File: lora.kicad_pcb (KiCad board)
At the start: 2 copper layers, 1 part, among them U1 SX1301

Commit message: partialy wired - sequential pins
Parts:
- added C2: 100nF, Capacitor_SMD:C_0603_1608Metric_Pad1.05x0.95mm_HandSolder, F.Cu at (154.5, 92.2)
- added C3: 100nF, Capacitor_SMD:C_0603_1608Metric_Pad1.05x0.95mm_HandSolder, F.Cu at (154.1, 88.9)
- added C4: 100nF, Capacitor_SMD:C_0603_1608Metric_Pad1.05x0.95mm_HandSolder, F.Cu at (157.9, 111.8)
- added C5: 100n, Capacitor_SMD:C_0603_1608Metric_Pad1.05x0.95mm_HandSolder, F.Cu at (158.4, 109.2)
- added C6: 100nF, Capacitor_SMD:C_0603_1608Metric_Pad1.05x0.95mm_HandSolder, F.Cu at (165.5, 100.7)
- added C7: 100n, Capacitor_SMD:C_0603_1608Metric_Pad1.05x0.95mm_HandSolder, F.Cu at (167.6, 100.7)
- added J1: Conn_01x10_Male, Connector_PinHeader_2.54mm:PinHeader_1x10_P2.54mm_Vertical, F.Cu at (139.0, 90.7)
- added R1: 10k, Resistor_SMD:R_0603_1608Metric_Pad1.05x0.95mm_HandSolder, F.Cu at (147.3, 100.7)
- added R10: 100, Resistor_SMD:R_0603_1608Metric_Pad1.05x0.95mm_HandSolder, F.Cu at (174.4, 95.2)
- added R2: 10k, Resistor_SMD:R_0603_1608Metric_Pad1.05x0.95mm_HandSolder, F.Cu at (146.8, 90.2)
- added R3: 100, Resistor_SMD:R_0603_1608Metric_Pad1.05x0.95mm_HandSolder, F.Cu at (174.4, 102.9)
- added R4: 100, Resistor_SMD:R_0603_1608Metric_Pad1.05x0.95mm_HandSolder, F.Cu at (178.2, 101.6)
- added R5: R, Resistor_SMD:R_0603_1608Metric_Pad1.05x0.95mm_HandSolder, F.Cu at (174.4, 100.3)
- added R6: 100, Resistor_SMD:R_0603_1608Metric_Pad1.05x0.95mm_HandSolder, F.Cu at (183.3, 100.3)
- added R7: 100, Resistor_SMD:R_0603_1608Metric_Pad1.05x0.95mm_HandSolder, F.Cu at (178.2, 99.1)
- added R8: 100, Resistor_SMD:R_0603_1608Metric_Pad1.05x0.95mm_HandSolder, F.Cu at (174.4, 97.8)
- added R9: 100, Resistor_SMD:R_0603_1608Metric_Pad1.05x0.95mm_HandSolder, F.Cu at (178.2, 96.5)
- moved U1 92.7 mm to (155.0, 100.4)
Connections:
- U1 pad 1: Net-(U1-Pad1) -> /RESET
- U1 pad 12: Net-(U1-Pad12) -> +1V8
- U1 pad 16: Net-(U1-Pad16) -> Earth
- U1 pad 2: Net-(U1-Pad2) -> /HOST_SCK
- U1 pad 23: Net-(U1-Pad23) -> +1V8
- U1 pad 29: Net-(U1-Pad29) -> +3V3
- U1 pad 32: Net-(U1-Pad32) -> Earth
- U1 pad 33: Net-(U1-Pad33) -> Earth
- U1 pad 34: Net-(U1-Pad34) -> Earth
- U1 pad 42: Net-(U1-Pad42) -> +1V8
- U1 pad 48: Net-(U1-Pad48) -> Earth
- U1 pad 49: Net-(U1-Pad49) -> Earth
- U1 pad 52: Net-(U1-Pad52) -> +3V3
- U1 pad 6: Net-(U1-Pad6) -> Earth
- U1 pad 60: Net-(U1-Pad60) -> +1V8
- U1 pad 8: Net-(U1-Pad8) -> +1V8
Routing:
- net +1V8: track 0.00 -> 3.21 mm
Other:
- net class 1V8 added: clearance 0.2, trace_width 0.25, via_dia 0.8, via_drill 0.4
- net class 3V3 added: clearance 0.2, trace_width 0.25, via_dia 0.8, via_drill 0.4

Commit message: v1.0
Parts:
- added C1: 1uF, Capacitor_SMD:C_0603_1608Metric, F.Cu at (134.6, 43.4)
- added C10: 2n2, Capacitor_SMD:C_0402_1005Metric, F.Cu at (114.7, 33.4)
- added C11: 22u, Capacitor_SMD:C_0603_1608Metric, F.Cu at (116.2, 45.1)
- added C12: 100nF, Capacitor_SMD:C_0402_1005Metric, F.Cu at (124.9, 56.7)
- added C8: 1u, Capacitor_SMD:C_0603_1608Metric, F.Cu at (114.2, 35.2)
- added C9: 10u, Capacitor_SMD:C_0603_1608Metric, F.Cu at (132.1, 40.4)
- added D1: LED, LED_SMD:LED_0402_1005Metric, F.Cu at (124.3, 34.7)
- added D2: LED, LED_SMD:LED_0402_1005Metric, F.Cu at (125.0, 36.9)
- added D3: LED, LED_SMD:LED_0402_1005Metric, F.Cu at (125.7, 34.7)
- added D4: LED, LED_SMD:LED_0402_1005Metric, F.Cu at (126.4, 36.9)
- added D5: LED, LED_SMD:LED_0402_1005Metric, F.Cu at (127.1, 34.7)
- added J2: Conn_Coaxial, Connector_Coaxial:U.FL_Molex_MCRF_73412-0110_Vertical, F.Cu at (116.2, 58.5)
- added J3: Conn_01x08_Male, Connector_PinHeader_2.54mm:PinHeader_1x08_P2.54mm_Vertical, B.Cu at (114.3, 63.5)
- added J4: Conn_01x10_Male, Connector_PinHeader_2.54mm:PinHeader_1x10_P2.54mm_Vertical, B.Cu at (139.7, 61.0)
- added J5: Conn_01x06_Male, Connector_PinHeader_2.54mm:PinHeader_1x06_P2.54mm_Vertical, B.Cu at (127.0, 30.5)
- added L1: 2.2uH, Inductor_SMD:L_6.3x6.3_H3, F.Cu at (117.5, 40.5)
- added R11: 100k, Resistor_SMD:R_0402_1005Metric, F.Cu at (121.0, 34.5)
- added R12: 100, Resistor_SMD:R_0402_1005Metric, F.Cu at (133.3, 56.7)
- added R13: 470, Resistor_SMD:R_0402_1005Metric, F.Cu at (127.1, 39.3)
- added R14: 470, Resistor_SMD:R_0402_1005Metric, F.Cu at (126.4, 41.8)
- added R15: 470, Resistor_SMD:R_0402_1005Metric, F.Cu at (125.7, 39.3)
- added R16: 470, Resistor_SMD:R_0402_1005Metric, F.Cu at (125.0, 41.9)
- added R17: 470, Resistor_SMD:R_0402_1005Metric, F.Cu at (124.3, 39.3)
- added R18: 0, Resistor_SMD:R_0402_1005Metric, F.Cu at (137.6, 53.0)
- added TP1: TestPoint, TestPoint:TestPoint_THTPad_1.5x1.5mm_Drill0.7mm, F.Cu at (131.7, 43.3)
- added TP3: TestPoint, TestPoint:TestPoint_THTPad_1.5x1.5mm_Drill0.7mm, F.Cu at (128.9, 39.8)
- added U2: TPS62141, Package_DFN_QFN:QFN-16-1EP_3x3mm_P0.5mm_EP1.8x1.8mm, F.Cu at (118.0, 34.5)
- added X1: DFA-S15, Oscillator:Oscillator_SMD_Fordahl_DFAS15-4Pin_5.0x3.2mm, F.Cu at (134.6, 52.9)
- added X2: ASE-xxxMHz, Oscillator:Oscillator_SMD_Abracon_ASE-4Pin_3.2x2.5mm, F.Cu at (130.9, 36.8)
- C2, C3, C4, C5, C6, C7: footprint Capacitor_SMD:C_0603_1608Metric_Pad1.05x0.95mm_HandSolder -> Capacitor_SMD:C_0402_1005Metric
- J1: moved to B.Cu
- R1, R10, R2, R3, R4, R6, R7, R8, R9: footprint Resistor_SMD:R_0603_1608Metric_Pad1.05x0.95mm_HandSolder -> Resistor_SMD:R_0402_1005Metric
- R5: value R -> 100; footprint Resistor_SMD:R_0603_1608Metric_Pad1.05x0.95mm_HandSolder -> Resistor_SMD:R_0402_1005Metric
- moved C4 77.4 mm to (123.6, 42.4), turned to 90 degrees
- moved C5 72.1 mm to (128.8, 43.5), turned to 0 degrees
- moved R6 70.8 mm to (134.4, 49.1), turned to 180 degrees
- moved R7 67.2 mm to (134.4, 48.1), turned to 180 degrees
- moved R9 66.8 mm to (134.4, 46.1), turned to 180 degrees
- moved R8 64.6 mm to (134.4, 47.1)
- moved R10 64.1 mm to (134.4, 45.1), turned to 180 degrees
- moved R2 62.7 mm to (113.4, 37.1), turned to 270 degrees
- moved R4 61.5 mm to (133.2, 59.6)
- moved C6 61.4 mm to (132.4, 49.0), turned to 0 degrees
- moved J1 59.3 mm to (111.6, 38.1), turned to 180 degrees
- moved R5 58.9 mm to (133.3, 58.1)
- moved U1 58.8 mm to (125.3, 49.6)
- moved C7 58.7 mm to (127.9, 57.4), turned to 270 degrees
- moved R3 58.7 mm to (133.2, 61.0)
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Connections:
- net /HOST_SCK renamed /SCK
- C2 pad 1: Earth -> +1V8
- C2 pad 2: +1V8 -> Earth
- C4 pad 1: +3V3 -> +1V8
- C5 pad 1: Earth -> +3V3
- C5 pad 2: +3V3 -> Earth
- C6 pad 1: Earth -> +1V8
- C6 pad 2: +1V8 -> Earth
- C7 pad 1: Earth -> +3V3
- C7 pad 2: +1V8 -> Earth
- J1 pad 10: Net-(J1-Pad10) -> /PA_G0
- J1 pad 3: Net-(J1-Pad3) -> /MISO
- J1 pad 4: Net-(J1-Pad4) -> /MOSI
- J1 pad 5: Net-(J1-Pad5) -> /CS
- J1 pad 6: Net-(J1-Pad6) -> /RA_EN
- J1 pad 7: Net-(J1-Pad7) -> /LA_CTR
- J1 pad 8: Net-(J1-Pad8) -> /PA_CTR
- J1 pad 9: Net-(J1-Pad9) -> /PA_G1
- R1 pad 1: Net-(J2-Pad1) -> Earth
- R1 pad 2: Earth -> Net-(J2-Pad1)
- U1 pad 13: Net-(U1-Pad13) -> /RA_EN
- U1 pad 14: Net-(U1-Pad14) -> /LA_CTR
- U1 pad 15: Net-(U1-Pad15) -> /PA_CTR
- U1 pad 17: Net-(U1-Pad17) -> /PA_G1
- U1 pad 18: Net-(U1-Pad18) -> /PA_G0
- U1 pad 3: Net-(U1-Pad3) -> /MISO
- U1 pad 34: Earth -> Net-(R3-Pad1)
- U1 pad 35: Net-(R3-Pad1) -> Net-(R4-Pad2)
- U1 pad 36: Net-(R4-Pad2) -> Net-(R5-Pad2)
- U1 pad 39: Net-(R5-Pad2) -> Net-(R12-Pad2)
- U1 pad 4: Net-(U1-Pad4) -> /MOSI
- U1 pad 5: Net-(U1-Pad5) -> /CS
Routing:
- net Earth: track 48.4 -> 213.0 mm, vias 0 -> 13
- net +1V8: track 3.21 -> 119.3 mm, vias 0 -> 8
- net +3V3: track 0.00 -> 76.6 mm, vias 0 -> 4
- net Net-(J5-Pad1): track 0.00 -> 18.1 mm
- net /RESET: track 0.00 -> 17.1 mm
- net Net-(J5-Pad4): track 0.00 -> 16.2 mm
- net Net-(J5-Pad2): track 0.00 -> 15.6 mm
- net Net-(J5-Pad3): track 0.00 -> 15.4 mm
- net /PA_G0: track 0.00 -> 14.8 mm
- net Net-(J3-Pad1): track 0.00 -> 14.4 mm
- net /SCK: track 0.00 -> 13.6 mm
- net Net-(J2-Pad1): track 0.00 -> 13.3 mm, vias 0 -> 2
- net /PA_G1: track 0.00 -> 12.2 mm
- net Net-(J3-Pad2): track 0.00 -> 12.1 mm
- net /MISO: track 0.00 -> 11.6 mm
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- added copper zone on B.Cu, net Earth
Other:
- board outline added: 31.6 x 36.6 mm
- net class 1V8: trace_width 0.25 -> 1
- net class 3V3: trace_width 0.25 -> 1
- net class Default: trace_width 0.125 -> 0.25
- board text added: "LoRa decoder (c) danman.eu v1.0"

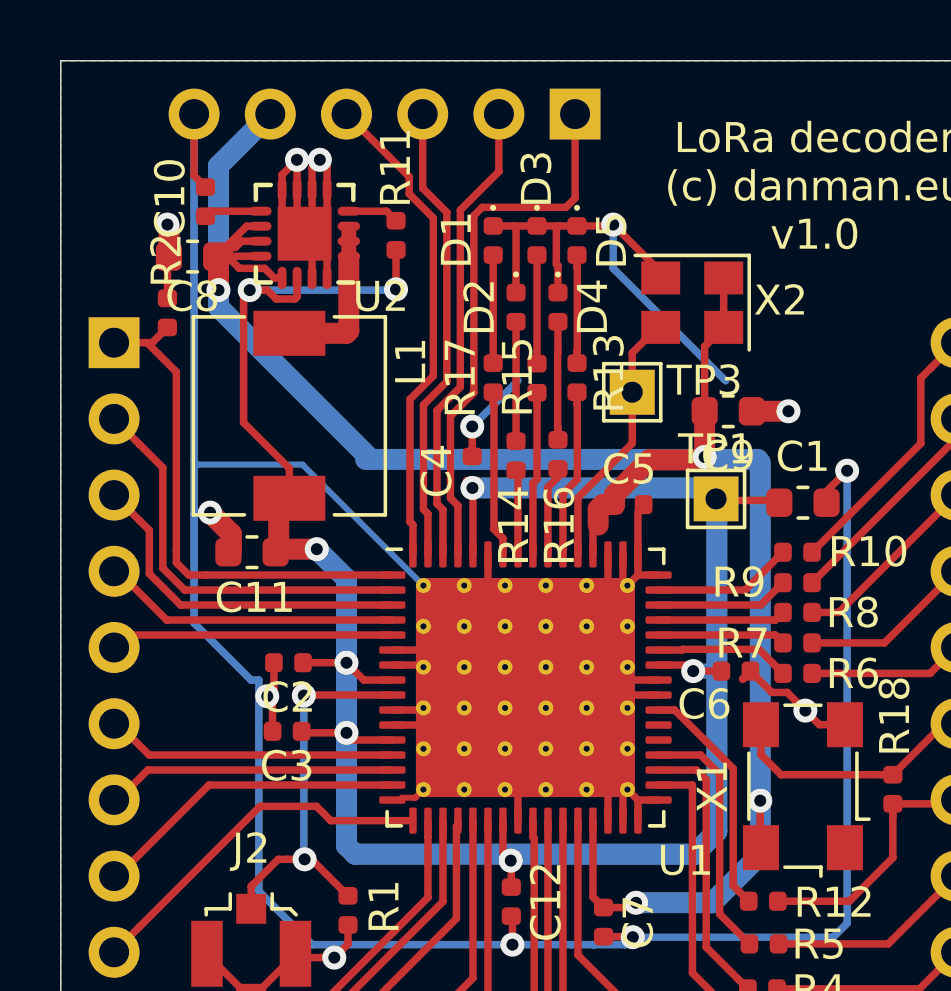
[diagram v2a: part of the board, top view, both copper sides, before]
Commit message: updated pcb TPS, values harmonization
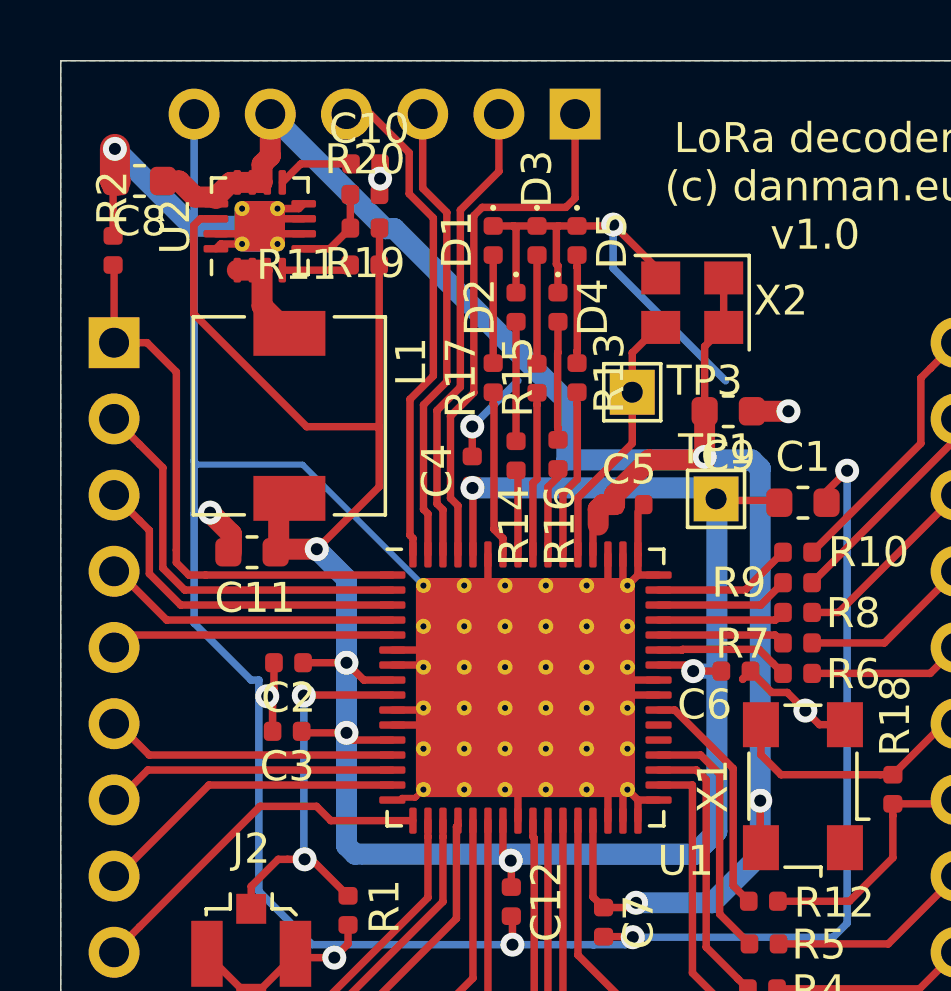
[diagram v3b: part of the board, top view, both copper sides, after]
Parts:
- added R19: R, Resistor_SMD:R_0402_1005Metric, F.Cu at (120.0, 34.3)
- added R20: R, Resistor_SMD:R_0402_1005Metric, F.Cu at (120.0, 33.2)
- U2: value TPS62141 -> TPS62140; footprint Package_DFN_QFN:QFN-16-1EP_3x3mm_P0.5mm_EP1.8x1.8mm -> Package_DFN_QFN:VQFN-16-1EP_3x3mm_P0.5mm_EP1.68x1.68mm_ThermalVias
- moved C10 5.48 mm to (120.0, 32.1), turned to 0 degrees
- moved C8 3.08 mm to (112.5, 32.7)
- moved R2 2.76 mm to (111.6, 35.0)
- moved U2 1.51 mm to (116.5, 34.2), turned to 90 degrees
- moved R11 1.44 mm to (120.0, 35.5), turned to 180 degrees
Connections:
- U2 pad 5: Earth -> Net-(R19-Pad2)
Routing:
- net +3V3: track 76.6 -> 68.8 mm, vias 4 -> 3
- net +1V8: track 119.3 -> 126.2 mm, vias 8 -> 6
- net Earth: track 213.0 -> 209.8 mm, vias 13 -> 12
- net Net-(L1-Pad1): track 6.40 -> 3.31 mm
- net Net-(R19-Pad2): track 0.00 -> 2.93 mm
- net /RESET: track 17.1 -> 18.8 mm
- net Net-(C10-Pad1): track 1.90 -> 2.55 mm
- net Net-(R11-Pad2): track 1.70 -> 2.33 mm

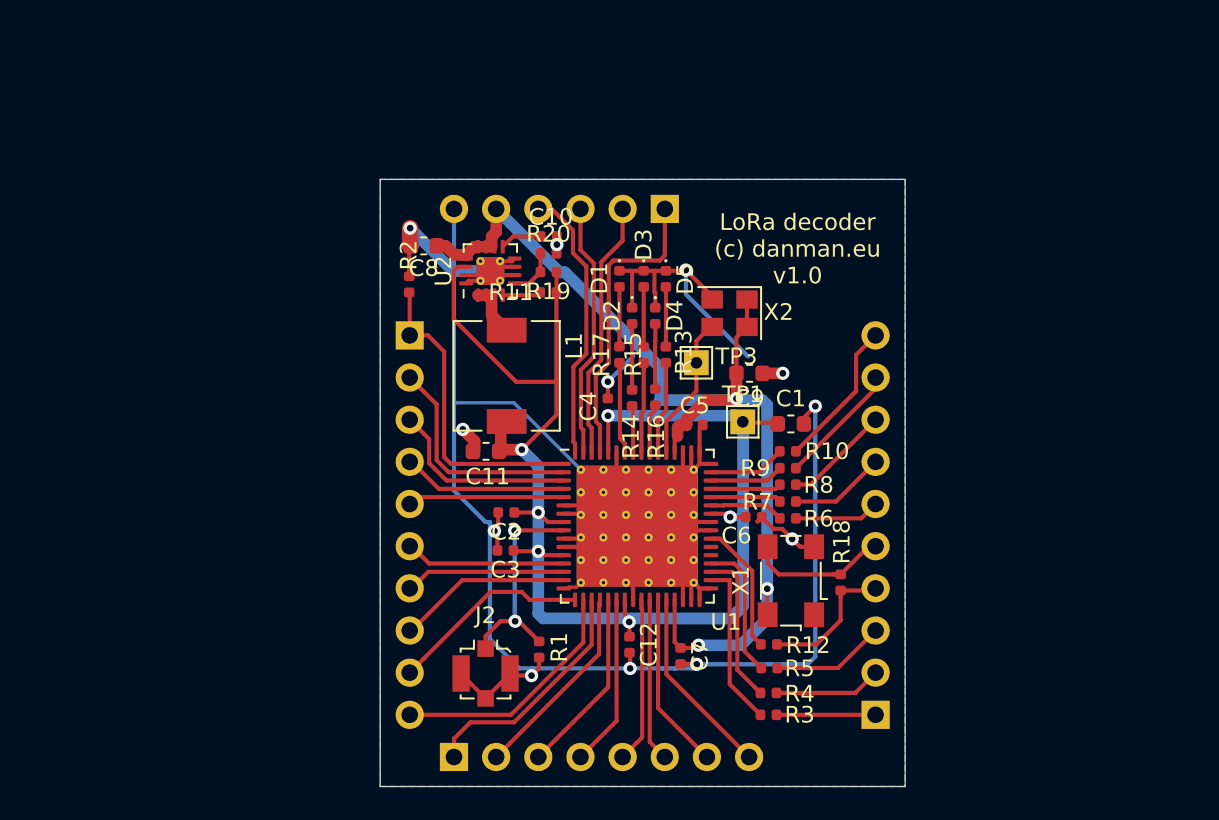
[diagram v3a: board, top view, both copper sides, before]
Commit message: two regulators, old connectors removed
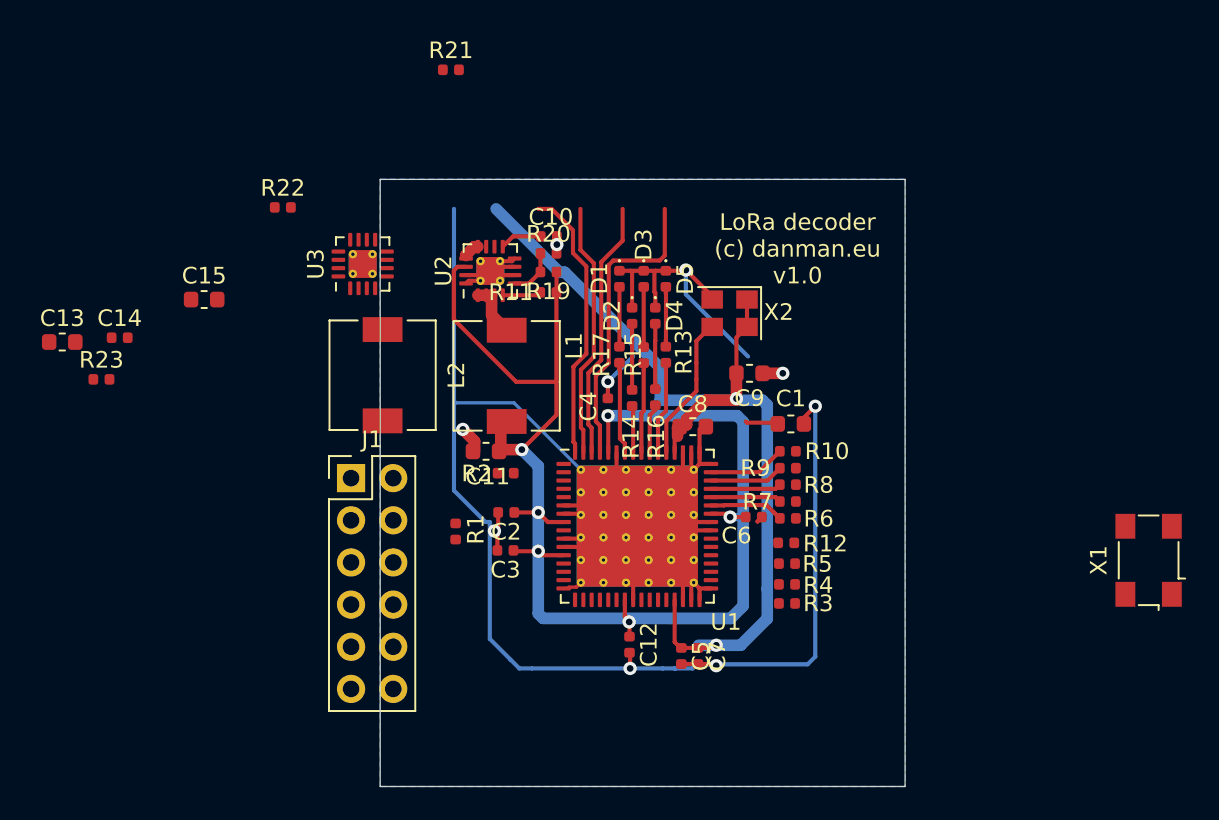
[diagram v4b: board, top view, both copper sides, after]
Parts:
- removed J2: Conn_Coaxial, Connector_Coaxial:U.FL_Molex_MCRF_73412-0110_Vertical
- removed J3: Conn_01x08_Male, Connector_PinHeader_2.54mm:PinHeader_1x08_P2.54mm_Vertical
- removed J4: Conn_01x10_Male, Connector_PinHeader_2.54mm:PinHeader_1x10_P2.54mm_Vertical
- removed J5: Conn_01x06_Male, Connector_PinHeader_2.54mm:PinHeader_1x06_P2.54mm_Vertical
- removed R18: 0, Resistor_SMD:R_0402_1005Metric
- removed TP1, TP3: TestPoint, TestPoint:TestPoint_THTPad_1.5x1.5mm_Drill0.7mm
- added C13: 10u, Capacitor_SMD:C_0603_1608Metric, F.Cu at (90.7, 38.5)
- added C14: 2n2, Capacitor_SMD:C_0402_1005Metric, F.Cu at (94.2, 38.2)
- added C15: 22u, Capacitor_SMD:C_0603_1608Metric, F.Cu at (99.2, 35.9)
- added L2: 2.2uH, Inductor_SMD:L_6.3x6.3_H3, F.Cu at (110.0, 40.5)
- added R21: 100k, Resistor_SMD:R_0402_1005Metric, F.Cu at (114.1, 22.1)
- added R22: R, Resistor_SMD:R_0402_1005Metric, F.Cu at (104.0, 30.4)
- added R23: R, Resistor_SMD:R_0402_1005Metric, F.Cu at (93.1, 40.8)
- added U3: TPS62140, Package_DFN_QFN:VQFN-16-1EP_3x3mm_P0.5mm_EP1.68x1.68mm_ThermalVias, F.Cu at (108.8, 33.8)
- C1: value 1uF -> 1u
- C12, C2, C3, C4, C6: value 100nF -> 100n
- J1: value Conn_01x10_Male -> Conn_02x06_Odd_Even; footprint Connector_PinHeader_2.54mm:PinHeader_1x10_P2.54mm_Vertical -> Connector_PinHeader_2.54mm:PinHeader_2x06_P2.54mm_Vertical; moved to F.Cu
- moved X1 21.6 mm to (156.2, 51.6)
- moved C8 19.5 mm to (128.7, 43.6), turned to 180 degrees
- moved C5 13.9 mm to (128.0, 57.4), turned to 270 degrees
- moved R2 12.8 mm to (117.4, 46.4), turned to 0 degrees
- moved J1 9.30 mm to (108.1, 46.7), turned to 0 degrees
- moved R1 8.71 mm to (114.4, 49.9)
- moved R3 6.80 mm to (134.4, 54.2)
- moved R4 6.63 mm to (134.4, 53.1)
- moved R5 6.38 mm to (134.4, 51.9)
- moved R12 6.21 mm to (134.3, 50.6)
- moved C7 1.05 mm to (129.0, 57.4)
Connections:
- C9 pad 1: +3V3 -> VCC
- J1 pad 1: /RESET -> Earth
- J1 pad 10: /PA_G0 -> /MOSI
- J1 pad 2: /SCK -> VCC
- J1 pad 3: /MISO -> Earth
- J1 pad 4: /MOSI -> +3V3
- J1 pad 5: /CS -> Earth
- J1 pad 6: /RA_EN -> +1V8
- J1 pad 7: /LA_CTR -> /RESET
- J1 pad 8: /PA_CTR -> /SCK
- J1 pad 9: /PA_G1 -> /MISO
- R1 pad 2: Net-(J2-Pad1) -> /GPS_IN
- U1 pad 9: Net-(J2-Pad1) -> /GPS_IN
- U2 pad 10: +3V3 -> VCC
- U2 pad 11: +3V3 -> VCC
- U2 pad 12: +3V3 -> VCC
- U2 pad 13: +3V3 -> VCC
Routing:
- net Earth: track 209.8 -> 191.0 mm, vias 12 -> 9
- net /RESET: track 18.8 -> 0.00 mm
- net /PA_G0: track 14.8 -> 0.00 mm
- net Net-(U1-Pad19): track 14.4 -> 0.00 mm
- net /SCK: track 13.6 -> 0.00 mm
- net Net-(J2-Pad1): track 13.3 -> 0.00 mm, vias 2 -> 0
- net /PA_G1: track 12.2 -> 0.00 mm
- net Net-(U1-Pad20): track 12.1 -> 0.00 mm
- net /MISO: track 11.6 -> 0.00 mm
- net Net-(U1-Pad28): track 11.5 -> 0.00 mm
- net Net-(U1-Pad21): track 11.2 -> 0.00 mm
- net Net-(U1-Pad27): track 10.7 -> 0.00 mm
- net /PA_CTR: track 10.4 -> 0.00 mm
- net Net-(U1-Pad22): track 10.4 -> 0.00 mm
- net Net-(R3-Pad1): track 10.0 -> 0.00 mm
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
